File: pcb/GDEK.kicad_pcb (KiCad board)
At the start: 2 copper layers, 276 x 118 mm, 326 parts, among them J1 TYPE-C-31-M-13C, J101 TYPE-C-31-M-13C, J102 AudioJack4, J103 Debug pads, J2 AudioJack4, J3 Debug pads, SW1 SW_Push_45deg, SW10 SW_Push_45deg, SW101 SW_Push_45deg, SW102 SW_Push_45deg, SW103 SW_Push_45deg, SW104 SW_Push_45deg, SW105 SW_Push_45deg, SW106 SW_Push_45deg, SW107 SW_Push_45deg, SW108 SW_Push_45deg, SW109 SW_Push_45deg, SW11 SW_Push_45deg, SW110 SW_Push_45deg, SW111 SW_Push_45deg, SW112 SW_Push_45deg, SW113 SW_Push_45deg, SW114 SW_Push_45deg, SW115 SW_Push_45deg, SW116 SW_Push_45deg, SW117 SW_Push_45deg, SW118 SW_Push_45deg, SW119 SW_Push_45deg, SW12 SW_Push_45deg, SW120 SW_Push_45deg, SW121 SW_Push_45deg, SW122 SW_Push_45deg, SW123 SW_Push_45deg, SW124 SW_Push_45deg, SW125 SW_Push_45deg, SW126 SW_Push_45deg, SW127 SW_Push_45deg, SW128 SW_Push_45deg, SW129 SW_Push_45deg, SW13 SW_Push_45deg, SW130 SW_Push_45deg, SW131 RotaryEncoder_Switch, SW14 SW_Push_45deg, SW15 SW_Push_45deg, SW16 SW_Push_45deg, SW17 SW_Push_45deg, SW18 SW_Push_45deg, SW19 SW_Push_45deg, SW2 SW_Push_45deg, SW20 SW_Push_45deg, SW21 SW_Push_45deg, SW22 SW_Push_45deg, SW23 SW_Push_45deg, SW24 SW_Push_45deg, SW25 SW_Push_45deg, SW26 SW_Push_45deg, SW27 SW_Push_45deg, SW28 SW_Push_45deg, SW29 SW_Push_45deg, SW3 SW_Push_45deg, SW30 SW_Push_45deg, SW31 RotaryEncoder_Switch, SW4 SW_Push_45deg, SW5 SW_Push_45deg, SW6 SW_Push_45deg, SW7 SW_Push_45deg, SW8 SW_Push_45deg, SW9 SW_Push_45deg, U1 RP2040, U101 RP2040, U102 W25Q128JVS, U103 74AHCT1G125, U104 USBLC6-2P6, U105 XC6210B332MR, U2 W25Q128JVS, U3 74AHCT1G125, U4 USBLC6-2P6, U5 XC6210B332MR, Y1 ABM8-272-T3, Y101 ABM8-272-T3

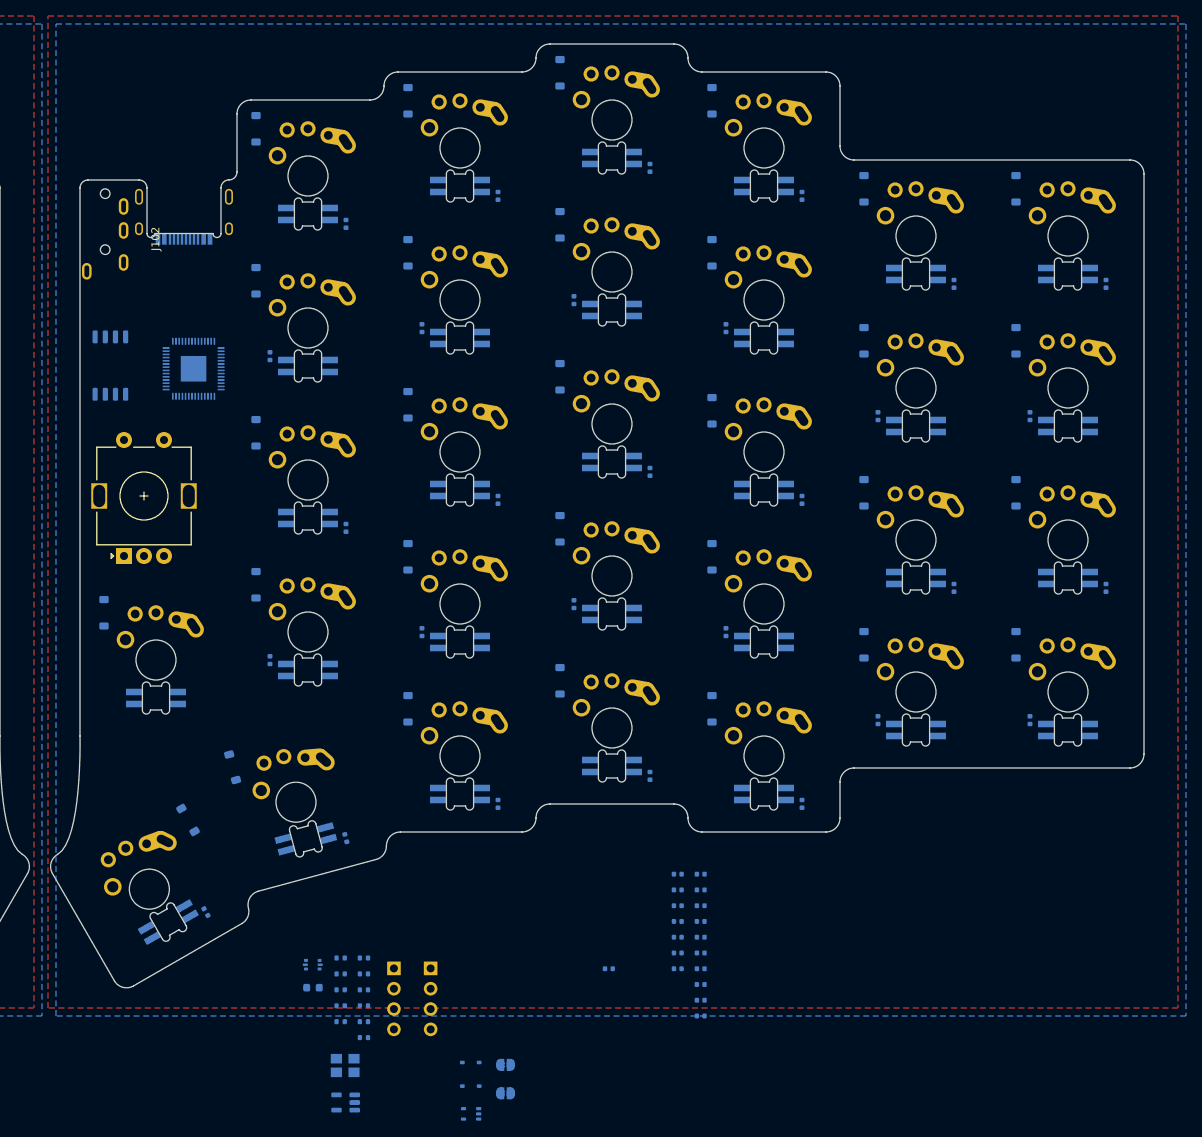
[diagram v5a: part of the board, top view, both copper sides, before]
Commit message: 🎨 Remove component references from silkscreen
YOLO.
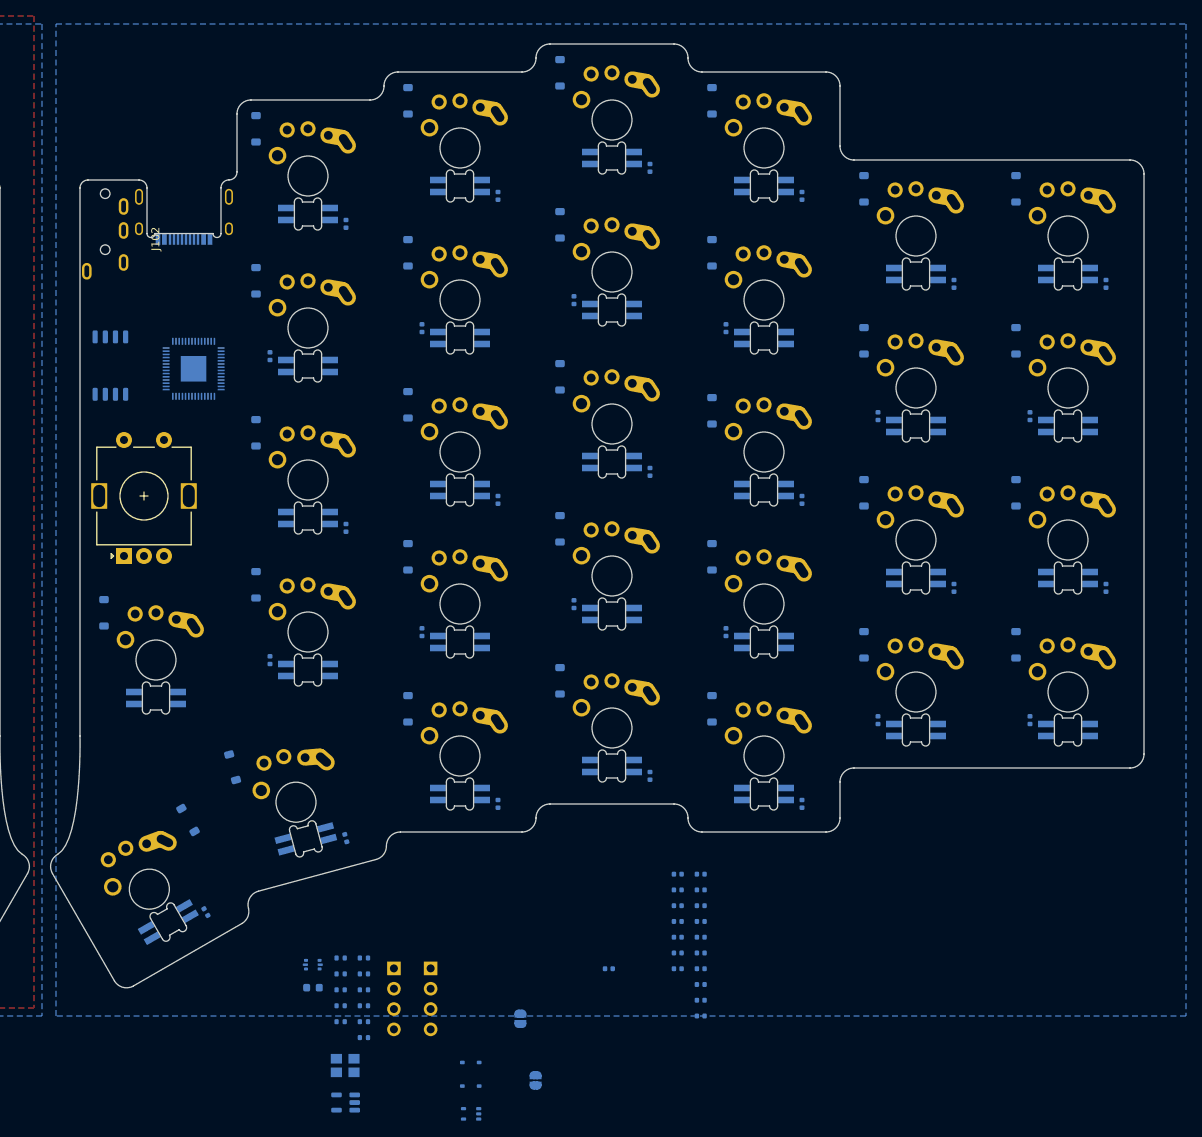
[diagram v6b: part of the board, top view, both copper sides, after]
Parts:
- moved R 6.05 mm to (218.1, 136.8), turned to -90 degrees
- moved B 4.09 mm to (219.9, 144.6), turned to -90 degrees
- renumbered TP2 to B, TP102 to B, TP1 to R, TP101 to R
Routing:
- removed copper zone on F.Cu, net GND_R
